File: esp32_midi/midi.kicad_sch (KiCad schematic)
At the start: 1 part

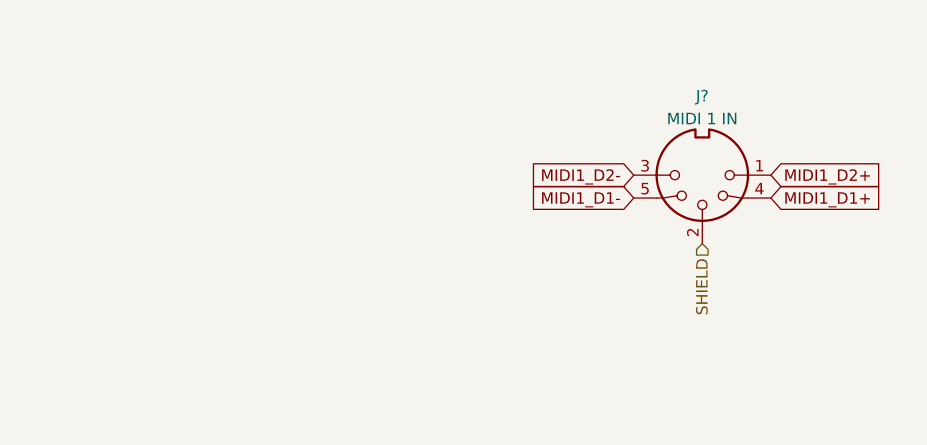
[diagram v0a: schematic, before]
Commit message: added midi thru
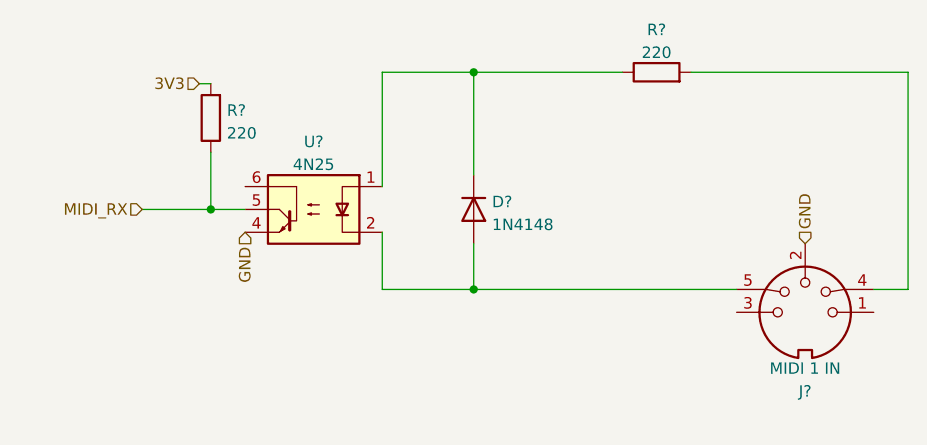
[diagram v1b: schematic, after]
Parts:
- added D?: 1N4148, symbol Device:D
- added R? (x2): 220, symbol Device:R
- added U?: 4N25, Package_DIP:DIP-6_W7.62mm, symbol Isolator:4N25
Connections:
- net MIDI1_D1+: no longer names the net of J?.4
- net MIDI1_D1+: now also R?.2
- net MIDI1_D1-: no longer names the net of J?.5
- net MIDI1_D1-: now also D?.2 (A), U?.2
- net MIDI1_D2+: no longer names the net of J?.1
- net MIDI1_D2-: no longer names the net of J?.3
- net SHIELD renamed GND
- net GND: now also U?.4
- new net: D?.1 (K), R?.1, U?.1
- new net 3V3: R?.2
- new net MIDI_RX: R?.1, U?.5
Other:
- moved on the sheet: J?
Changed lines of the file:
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@@
 (kicad_sch (version 20211123) (generator eeschema)
   (paper "A4")
-  (global_label "MIDI1_D2+" (shape input) (at 125.73 62.23 0) (fields_autoplaced)
+  (junction (at 63.5 66.04) (diameter 0) (color 0 0 0 0)
+  )
+  (junction (at 92.71 74.93) (diameter 0) (color 0 0 0 0)
+  )
+  (junction (at 92.71 50.8) (diameter 0) (color 0 0 0 0)
+  )
+  (wire (pts (xy 63.5 66.04) (xy 67.31 66.04))
+    (stroke (width 0) (type default) (color 0 0 0 0))
+  )
+  (wire (pts (xy 121.92 74.93) (xy 92.71 74.93))
+    (stroke (width 0) (type default) (color 0 0 0 0))
+  )
+  (wire (pts (xy 137.16 74.93) (xy 140.97 74.93))
+    (stroke (width 0) (type default) (color 0 0 0 0))
+  )
+  (wire (pts (xy 63.5 59.69) (xy 63.5 66.04))
+    (stroke (width 0) (type default) (color 0 0 0 0))
+  )
+  (wire (pts (xy 140.97 50.8) (xy 116.84 50.8))
+    (stroke (width 0) (type default) (color 0 0 0 0))
+  )
+  (wire (pts (xy 140.97 74.93) (xy 140.97 50.8))
+    (stroke (width 0) (type default) (color 0 0 0 0))
+  )
+  (wire (pts (xy 62.23 52.07) (xy 63.5 52.07))
+    (stroke (width 0) (type default) (color 0 0 0 0))
+  )
+  (wire (pts (xy 82.55 50.8) (xy 82.55 63.5))
+    (stroke (width 0) (type default) (color 0 0 0 0))
+  )
+  (wire (pts (xy 55.88 66.04) (xy 63.5 66.04))
+    (stroke (width 0) (type default) (color 0 0 0 0))
+  )
+  (wire (pts (xy 109.22 50.8) (xy 92.71 50.8))
+    (stroke (width 0) (type default) (color 0 0 0 0))
+  )
+  (wire (pts (xy 92.71 74.93) (xy 82.55 74.93))
+    (stroke (width 0) (type default) (color 0 0 0 0))
+  )
+  (wire (pts (xy 92.71 50.8) (xy 92.71 62.23))
+    (stroke (width 0) (type default) (color 0 0 0 0))
+  )
+  (wire (pts (xy 92.71 69.85) (xy 92.71 74.93))
+    (stroke (width 0) (type default) (color 0 0 0 0))
+  )
+  (wire (pts (xy 82.55 74.93) (xy 82.55 68.58))
+    (stroke (width 0) (type default) (color 0 0 0 0))
+  )
+  (wire (pts (xy 92.71 50.8) (xy 82.55 50.8))
+    (stroke (width 0) (type default) (color 0 0 0 0))
+  )
+  (hierarchical_label "3V3" (shape input) (at 62.23 52.07 180)
+    (effects (font (size 1.27 1.27)) (justify right))
+  )
+  (hierarchical_label "MIDI_RX" (shape input) (at 55.88 66.04 180)
+    (effects (font (size 1.27 1.27)) (justify right))
+  )
+  (hierarchical_label "GND" (shape input) (at 129.54 69.85 90)
     (effects (font (size 1.27 1.27)) (justify left))
-    (property "Intersheet References" "${INTERSHEET_REFS}" (id 0) (at 138.3031 62.1506 0)
+  )
+  (hierarchical_label "GND" (shape input) (at 67.31 68.58 270)
+    (effects (font (size 1.27 1.27)) (justify right))
+  )
+  (symbol (lib_id "Device:D") (at 92.71 66.04 270) (unit 1)
+    (in_bom yes) (on_board yes) (fields_autoplaced)
+    (property "Reference" "D?" (id 0) (at 94.742 65.2053 90)
+      (effects (font (size 1.27 1.27)) (justify left))
+    )
+    (property "Value" "1N4148" (id 1) (at 94.742 67.7422 90)
+      (effects (font (size 1.27 1.27)) (justify left))
+    )
+    (property "Footprint" "" (id 2) (at 92.71 66.04 0)
+      (effects (font (size 1.27 1.27)) hide)
+    )
+    (property "Datasheet" "~" (id 3) (at 92.71 66.04 0)
+      (effects (font (size 1.27 1.27)) hide)
+    )
+    (pin "1")
+    (pin "2")
+  )
+  (symbol (lib_id "Device:R") (at 63.5 55.88 180) (unit 1)
+    (in_bom yes) (on_board yes) (fields_autoplaced)
+    (property "Reference" "R?" (id 0) (at 65.278 55.0453 0)
+      (effects (font (size 1.27 1.27)) (justify right))
+    )
+    (property "Value" "220" (id 1) (at 65.278 57.5822 0)
+      (effects (font (size 1.27 1.27)) (justify right))
+    )
+    (property "Footprint" "" (id 2) (at 65.278 55.88 90)
+      (effects (font (size 1.27 1.27)) hide)
+    )
+    (property "Datasheet" "~" (id 3) (at 63.5 55.88 0)
+      (effects (font (size 1.27 1.27)) hide)
+    )
+    (pin "1")
+    (pin "2")
+  )
+  (symbol (lib_id "Isolator:4N25") (at 74.93 66.04 0) (mirror y) (unit 1)
+    (in_bom yes) (on_board yes) (fields_autoplaced)
+    (property "Reference" "U?" (id 0) (at 74.93 58.5302 0))
+    (property "Value" "4N25" (id 1) (at 74.93 61.0671 0))
+    (property "Footprint" "Package_DIP:DIP-6_W7.62mm" (id 2) (at 80.01 71.12 0)
+      (effects (font (size 1.27 1.27) italic) (justify left) hide)
+    )
+    (property "Datasheet" "https://www.vishay.com/docs/83725/4n25.pdf" (id 3) (at 74.93 66.04 0)
       (effects (font (size 1.27 1.27)) (justify left) hide)
     )
+    (pin "1")
+    (pin "2")
+    (pin "3")
+    (pin "4")
+    (pin "5")
+    (pin "6")
   )
-  (global_label "MIDI1_D1-" (shape input) (at 110.49 64.77 180) (fields_autoplaced)
-    (effects (font (size 1.27 1.27)) (justify right))
-    (property "Intersheet References" "${INTERSHEET_REFS}" (id 0) (at 97.9169 64.6906 0)
-      (effects (font (size 1.27 1.27)) (justify right) hide)
-    )
-  )
-  (global_label "MIDI1_D2-" (shape input) (at 110.49 62.23 180) (fields_autoplaced)
-    (effects (font (size 1.27 1.27)) (justify right))
-    (property "Intersheet References" "${INTERSHEET_REFS}" (id 0) (at 97.9169 62.1506 0)
-      (effects (font (size 1.27 1.27)) (justify right) hide)
-    )
-  )
-  (global_label "MIDI1_D1+" (shape input) (at 125.73 64.77 0) (fields_autoplaced)
-    (effects (font (size 1.27 1.27)) (justify left))
-    (property "Intersheet References" "${INTERSHEET_REFS}" (id 0) (at 138.3031 64.6906 0)
-      (effects (font (size 1.27 1.27)) (justify left) hide)
-    )
-  )
-  (hierarchical_label "SHIELD" (shape input) (at 118.11 69.85 270)
-    (effects (font (size 1.27 1.27)) (justify right))
-  )
-  (symbol (lib_id "Connector:DIN-5_180degree") (at 118.11 62.23 180) (unit 1)
+  (symbol (lib_id "Device:R") (at 113.03 50.8 90) (unit 1)
     (in_bom yes) (on_board yes) (fields_autoplaced)
-    (property "Reference" "J?" (id 0) (at 118.1099 53.4502 0))
-    (property "Value" "MIDI 1 IN" (id 1) (at 118.1099 55.9871 0))
-    (property "Footprint" "" (id 2) (at 118.11 62.23 0)
+    (property "Reference" "R?" (id 0) (at 113.03 46.0842 90))
+    (property "Value" "220" (id 1) (at 113.03 48.6211 90))
+    (property "Footprint" "" (id 2) (at 113.03 52.578 90)
       (effects (font (size 1.27 1.27)) hide)
     )
-    (property "Datasheet" "http://www.mouser.com/ds/2/18/40_c091_abd_e-75918.pdf" (id 3) (at 118.11 62.23 0)
+    (property "Datasheet" "~" (id 3) (at 113.03 50.8 0)
       (effects (font (size 1.27 1.27)) hide)
     )
+    (pin "1")
+    (pin "2")
+  )
+  (symbol (lib_id "Connector:DIN-5_180degree") (at 129.54 77.47 0) (mirror y) (unit 1)
+    (in_bom yes) (on_board yes) (fields_autoplaced)
+    (property "Reference" "J?" (id 0) (at 129.5399 86.2498 0))
+    (property "Value" "MIDI 1 IN" (id 1) (at 129.5399 83.7129 0))
+    (property "Footprint" "" (id 2) (at 129.54 77.47 0)
+      (effects (font (size 1.27 1.27)) hide)
+    )
+    (property "Datasheet" "http://www.mouser.com/ds/2/18/40_c091_abd_e-75918.pdf" (id 3) (at 129.54 77.47 0)
+      (effects (font (size 1.27 1.27)) hide)
+    )

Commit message: work in progress, added usb-c flasher, add display connector, add midi connections
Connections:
- net 3V3: now also U?.5; no longer R?.2
- net GND: now also R?.1; no longer U?.4
- net MIDI_RX: now also R?.2, U?.4; no longer R?.1, U?.5
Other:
- moved on the sheet: R?

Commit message: More footprints applied
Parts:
- D9: renamed from D?; footprint (none) -> Diode_SMD:D_SOD-123
- J5: renamed from J?; footprint (none) -> ordentliche-teile:scheißmidi
- R3, R4: renamed from R?; footprint (none) -> Resistor_SMD:R_0402_1005Metric
- gave numbers to parts that had none: 1
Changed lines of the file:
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@@
   (symbol (lib_id "Device:D") (at 92.71 66.04 270) (unit 1)
     (in_bom yes) (on_board yes) (dnp no) (fields_autoplaced)
-    (property "Reference" "D?" (at 94.742 65.2053 90)
+    (property "Reference" "D9" (at 94.742 65.2053 90)
       (effects (font (size 1.27 1.27)) (justify left))
     )
@@
       (effects (font (size 1.27 1.27)) (justify left))
     )
-    (property "Footprint" "" (at 92.71 66.04 0)
+    (property "Footprint" "Diode_SMD:D_SOD-123" (at 92.71 66.04 0)
       (effects (font (size 1.27 1.27)) hide)
     )
@@
       (project "esp32_midi"
         (path "/e33c0603-5c0d-4712-ab63-5756d1504b4c/6690eb41-2c1d-4abf-90f8-fc4c3740650e/c474a483-652e-46b3-829f-20d9c40cc74b"
-          (reference "D?") (unit 1)
+          (reference "D9") (unit 1)
         )
       )
@@
   (symbol (lib_id "Device:R") (at 60.96 72.39 180) (unit 1)
     (in_bom yes) (on_board yes) (dnp no) (fields_autoplaced)
-    (property "Reference" "R?" (at 62.738 71.5553 0)
+    (property "Reference" "R3" (at 62.738 71.5553 0)
       (effects (font (size 1.27 1.27)) (justify right))
     )
@@
       (effects (font (size 1.27 1.27)) (justify right))
     )
-    (property "Footprint" "" (at 62.738 72.39 90)
+    (property "Footprint" "Resistor_SMD:R_0402_1005Metric" (at 62.738 72.39 90)
       (effects (font (size 1.27 1.27)) hide)
     )
@@
       (project "esp32_midi"
         (path "/e33c0603-5c0d-4712-ab63-5756d1504b4c/6690eb41-2c1d-4abf-90f8-fc4c3740650e/c474a483-652e-46b3-829f-20d9c40cc74b"
-          (reference "R?") (unit 1)
+          (reference "R3") (unit 1)
         )
       )
@@
   (symbol (lib_id "Isolator:4N25") (at 74.93 66.04 0) (mirror y) (unit 1)
     (in_bom yes) (on_board yes) (dnp no) (fields_autoplaced)
-    (property "Reference" "U?" (at 74.93 58.5302 0)
+    (property "Reference" "U9" (at 74.93 58.5302 0)
       (effects (font (size 1.27 1.27)))
     )
@@
       (project "esp32_midi"
         (path "/e33c0603-5c0d-4712-ab63-5756d1504b4c/6690eb41-2c1d-4abf-90f8-fc4c3740650e/c474a483-652e-46b3-829f-20d9c40cc74b"
-          (reference "U?") (unit 1)
+          (reference "U9") (unit 1)
         )
       )
@@
   (symbol (lib_id "Device:R") (at 113.03 50.8 90) (unit 1)
     (in_bom yes) (on_board yes) (dnp no) (fields_autoplaced)
-    (property "Reference" "R?" (at 113.03 46.0842 90)
+    (property "Reference" "R4" (at 113.03 46.0842 90)
       (effects (font (size 1.27 1.27)))
     )
@@
       (effects (font (size 1.27 1.27)))
     )
-    (property "Footprint" "" (at 113.03 52.578 90)
+    (property "Footprint" "Resistor_SMD:R_0402_1005Metric" (at 113.03 52.578 90)
       (effects (font (size 1.27 1.27)) hide)
     )
@@
       (project "esp32_midi"
         (path "/e33c0603-5c0d-4712-ab63-5756d1504b4c/6690eb41-2c1d-4abf-90f8-fc4c3740650e/c474a483-652e-46b3-829f-20d9c40cc74b"
-          (reference "R?") (unit 1)
+          (reference "R4") (unit 1)
         )
       )
@@
   (symbol (lib_id "Connector:DIN-5_180degree") (at 129.54 77.47 0) (mirror y) (unit 1)
     (in_bom yes) (on_board yes) (dnp no) (fields_autoplaced)
-    (property "Reference" "J?" (at 129.5399 86.2498 0)
+    (property "Reference" "J5" (at 129.5399 86.2498 0)
       (effects (font (size 1.27 1.27)))
     )
@@
       (effects (font (size 1.27 1.27)))
     )
-    (property "Footprint" "" (at 129.54 77.47 0)
+    (property "Footprint" "ordentliche-teile:scheißmidi" (at 129.54 77.47 0)
       (effects (font (size 1.27 1.27)) hide)
     )
@@
       (project "esp32_midi"
         (path "/e33c0603-5c0d-4712-ab63-5756d1504b4c/6690eb41-2c1d-4abf-90f8-fc4c3740650e/c474a483-652e-46b3-829f-20d9c40cc74b"
-          (reference "J?") (unit 1)
+          (reference "J5") (unit 1)
         )
       )

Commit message: Updated pcb
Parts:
- renumbered D9 to D5, U9 to U4
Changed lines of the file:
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@@
   (symbol (lib_id "Device:D") (at 92.71 66.04 270) (unit 1)
     (in_bom yes) (on_board yes) (dnp no) (fields_autoplaced)
-    (property "Reference" "D9" (at 94.742 65.2053 90)
+    (property "Reference" "D5" (at 94.742 65.2053 90)
       (effects (font (size 1.27 1.27)) (justify left))
     )
@@
       (project "esp32_midi"
         (path "/e33c0603-5c0d-4712-ab63-5756d1504b4c/6690eb41-2c1d-4abf-90f8-fc4c3740650e/c474a483-652e-46b3-829f-20d9c40cc74b"
-          (reference "D9") (unit 1)
+          (reference "D5") (unit 1)
         )
       )
@@
   (symbol (lib_id "Isolator:4N25") (at 74.93 66.04 0) (mirror y) (unit 1)
     (in_bom yes) (on_board yes) (dnp no) (fields_autoplaced)
-    (property "Reference" "U9" (at 74.93 58.5302 0)
+    (property "Reference" "U4" (at 74.93 58.5302 0)
       (effects (font (size 1.27 1.27)))
     )
@@
       (project "esp32_midi"
         (path "/e33c0603-5c0d-4712-ab63-5756d1504b4c/6690eb41-2c1d-4abf-90f8-fc4c3740650e/c474a483-652e-46b3-829f-20d9c40cc74b"
-          (reference "U9") (unit 1)
+          (reference "U4") (unit 1)
         )
       )

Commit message: More pcb
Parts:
- R3, R4: footprint Resistor_SMD:R_0402_1005Metric -> Resistor_SMD:R_1206_3216Metric
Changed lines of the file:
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@@
       (effects (font (size 1.27 1.27)) (justify right))
     )
-    (property "Footprint" "Resistor_SMD:R_0402_1005Metric" (at 62.738 72.39 90)
+    (property "Footprint" "Resistor_SMD:R_1206_3216Metric" (at 62.738 72.39 90)
       (effects (font (size 1.27 1.27)) hide)
     )
@@
       (effects (font (size 1.27 1.27)))
     )
-    (property "Footprint" "Resistor_SMD:R_0402_1005Metric" (at 113.03 52.578 90)
+    (property "Footprint" "Resistor_SMD:R_1206_3216Metric" (at 113.03 52.578 90)
       (effects (font (size 1.27 1.27)) hide)
     )

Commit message: Everything changed
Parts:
- added D6: LED, LED_SMD:LED_0603_1608Metric, symbol Device:LED
- added R11: 1k, Resistor_SMD:R_1206_3216Metric, symbol Device:R
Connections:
- net GND: now also R11.1
- net MIDI_RX: now also D6.1 (K)
- new net: D6.2 (A), R11.2
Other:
- moved on the sheet: R3
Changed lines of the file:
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@@
-(kicad_sch (version 20230121) (generator eeschema)
+(kicad_sch (version 20230620) (generator eeschema)
   (paper "A4")
   (junction (at 92.71 74.93) (diameter 0) (color 0 0 0 0)
   )
-  (junction (at 60.96 68.58) (diameter 0) (color 0 0 0 0)
+  (junction (at 57.15 68.58) (diameter 0) (color 0 0 0 0)
+  )
+  (junction (at 64.77 68.58) (diameter 0) (color 0 0 0 0)
   )
   (junction (at 92.71 50.8) (diameter 0) (color 0 0 0 0)
   )
-  (wire (pts (xy 60.96 68.58) (xy 67.31 68.58))
-    (stroke (width 0) (type default))
-  )
   (wire (pts (xy 121.92 74.93) (xy 92.71 74.93))
     (stroke (width 0) (type default))
@@
     (stroke (width 0) (type default))
   )
-  (wire (pts (xy 55.88 66.04) (xy 58.42 66.04))
-    (stroke (width 0) (type default))
-  )
-  (wire (pts (xy 58.42 68.58) (xy 60.96 68.58))
+  (wire (pts (xy 53.34 68.58) (xy 57.15 68.58))
+    (stroke (width 0) (type default))
+  )
+  (wire (pts (xy 57.15 68.58) (xy 64.77 68.58))
     (stroke (width 0) (type default))
   )
@@
     (stroke (width 0) (type default))
   )
+  (wire (pts (xy 64.77 68.58) (xy 67.31 68.58))
+    (stroke (width 0) (type default))
+  )
   (wire (pts (xy 92.71 69.85) (xy 92.71 74.93))
     (stroke (width 0) (type default))
@@
     (stroke (width 0) (type default))
   )
-  (wire (pts (xy 58.42 66.04) (xy 58.42 68.58))
-    (stroke (width 0) (type default))
-  )
   (wire (pts (xy 92.71 50.8) (xy 82.55 50.8))
     (stroke (width 0) (type default))
@@
     (stroke (width 0) (type default))
   )
-  (hierarchical_label "GND" (shape input) (at 60.96 76.2 270) (fields_autoplaced)
+  (hierarchical_label "GND" (shape input) (at 57.15 76.2 270) (fields_autoplaced)
     (effects (font (size 1.27 1.27)) (justify right))
   )
@@
     (effects (font (size 1.27 1.27)) (justify right))
   )
-  (hierarchical_label "MIDI_RX" (shape input) (at 55.88 66.04 180) (fields_autoplaced)
+  (hierarchical_label "MIDI_RX" (shape input) (at 53.34 68.58 180) (fields_autoplaced)
     (effects (font (size 1.27 1.27)) (justify right))
   )
@@
     (effects (font (size 1.27 1.27)) (justify left))
   )
+  (hierarchical_label "GND" (shape input) (at 64.77 83.82 270) (fields_autoplaced)
+    (effects (font (size 1.27 1.27)) (justify right))
+  )
   (symbol (lib_id "Device:D") (at 92.71 66.04 270) (unit 1)
     (in_bom yes) (on_board yes) (dnp no) (fields_autoplaced)
@@
       (effects (font (size 1.27 1.27)) hide)
     )
+    (property "Description" "" (at 92.71 66.04 0)
+      (effects (font (size 1.27 1.27)) hide)
+    )
     (pin "1")
     (pin "2")
@@
     )
   )
-  (symbol (lib_id "Device:R") (at 60.96 72.39 180) (unit 1)
-    (in_bom yes) (on_board yes) (dnp no) (fields_autoplaced)
-    (property "Reference" "R3" (at 62.738 71.5553 0)
-      (effects (font (size 1.27 1.27)) (justify right))
-    )
-    (property "Value" "220" (at 62.738 74.0922 0)
-      (effects (font (size 1.27 1.27)) (justify right))
-    )
-    (property "Footprint" "Resistor_SMD:R_1206_3216Metric" (at 62.738 72.39 90)
-      (effects (font (size 1.27 1.27)) hide)
-    )
-    (property "Datasheet" "~" (at 60.96 72.39 0)
+  (symbol (lib_id "Device:R") (at 57.15 72.39 180) (unit 1)
+    (in_bom yes) (on_board yes) (dnp no) (fields_autoplaced)
+    (property "Reference" "R3" (at 58.928 71.5553 0)
+      (effects (font (size 1.27 1.27)) (justify right))
+    )
+    (property "Value" "220" (at 58.928 74.0922 0)
+      (effects (font (size 1.27 1.27)) (justify right))
+    )
+    (property "Footprint" "Resistor_SMD:R_1206_3216Metric" (at 58.928 72.39 90)
+      (effects (font (size 1.27 1.27)) hide)
+    )
+    (property "Datasheet" "~" (at 57.15 72.39 0)
+      (effects (font (size 1.27 1.27)) hide)
+    )
+    (property "Description" "" (at 57.15 72.39 0)
       (effects (font (size 1.27 1.27)) hide)
     )
@@
     (property "Datasheet" "https://www.vishay.com/docs/83725/4n25.pdf" (at 74.93 66.04 0)
       (effects (font (size 1.27 1.27)) (justify left) hide)
+    )
+    (property "Description" "" (at 74.93 66.04 0)
+      (effects (font (size 1.27 1.27)) hide)
     )
     (pin "1")
@@
     )
   )
+  (symbol (lib_id "Device:R") (at 64.77 80.01 180) (unit 1)
+    (in_bom yes) (on_board yes) (dnp no)
+    (property "Reference" "R11" (at 62.23 80.01 90)
+      (effects (font (size 1.27 1.27)) (justify left))
+    )
+    (property "Value" "1k" (at 62.23 77.47 90)
+      (effects (font (size 1.27 1.27)) (justify left))
+    )
+    (property "Footprint" "Resistor_SMD:R_1206_3216Metric" (at 66.548 80.01 90)
+      (effects (font (size 1.27 1.27)) hide)
+    )
+    (property "Datasheet" "~" (at 64.77 80.01 0)
+      (effects (font (size 1.27 1.27)) hide)
+    )
+    (property "Description" "" (at 64.77 80.01 0)
+      (effects (font (size 1.27 1.27)) hide)
+    )
+    (property "LCSC Part #" "C11702" (at 64.77 80.01 0)
+      (effects (font (size 1.27 1.27)) hide)
+    )
+    (pin "1")
+    (pin "2")
+    (instances
+      (project "esp32_midi"
+        (path "/e33c0603-5c0d-4712-ab63-5756d1504b4c/2c215fe4-7c9a-4ae0-9a5d-913b04975b72"
+          (reference "R11") (unit 1)
+        )
+        (path "/e33c0603-5c0d-4712-ab63-5756d1504b4c/6690eb41-2c1d-4abf-90f8-fc4c3740650e/c474a483-652e-46b3-829f-20d9c40cc74b"
+          (reference "R101") (unit 1)
+        )
+      )
+    )
+  )
+  (symbol (lib_id "Device:LED") (at 64.77 72.39 270) (unit 1)
+    (in_bom yes) (on_board yes) (dnp no)
+    (property "Reference" "D6" (at 67.9766 74.6126 0)
+      (effects (font (size 1.27 1.27)) (justify right))
+    )
+    (property "Value" "LED" (at 66.2548 72.1082 0)
+      (effects (font (size 1.27 1.27)) (justify right))
+    )
+    (property "Footprint" "LED_SMD:LED_0603_1608Metric" (at 64.77 72.39 0)
+      (effects (font (size 1.27 1.27)) hide)
+    )
+    (property "Datasheet" "~" (at 64.77 72.39 0)
+      (effects (font (size 1.27 1.27)) hide)
+    )
+    (property "Description" "" (at 64.77 72.39 0)
+      (effects (font (size 1.27 1.27)) hide)
+    )
+    (property "LCSC Part #" "C2290" (at 64.77 72.39 0)
+      (effects (font (size 1.27 1.27)) hide)
+    )
+    (pin "1")
+    (pin "2")
+    (instances
+      (project "esp32_midi"
+        (path "/e33c0603-5c0d-4712-ab63-5756d1504b4c/2c215fe4-7c9a-4ae0-9a5d-913b04975b72"
+          (reference "D6") (unit 1)
+        )
+        (path "/e33c0603-5c0d-4712-ab63-5756d1504b4c/6690eb41-2c1d-4abf-90f8-fc4c3740650e/c474a483-652e-46b3-829f-20d9c40cc74b"
+          (reference "D237") (unit 1)
+        )
+      )
+    )
+  )
   (symbol (lib_id "Device:R") (at 113.03 50.8 90) (unit 1)
     (in_bom yes) (on_board yes) (dnp no) (fields_autoplaced)
@@
       (effects (font (size 1.27 1.27)) hide)
     )
+    (property "Description" "" (at 113.03 50.8 0)
+      (effects (font (size 1.27 1.27)) hide)
+    )
     (pin "1")
     (pin "2")
@@
       (effects (font (size 1.27 1.27)) hide)
     )
+    (property "Description" "" (at 129.54 77.47 0)
+      (effects (font (size 1.27 1.27)) hide)
+    )
